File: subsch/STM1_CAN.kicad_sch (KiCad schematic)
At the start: 13 parts, among them U7 STM32F072C8Tx, U8 TJA1051T-3

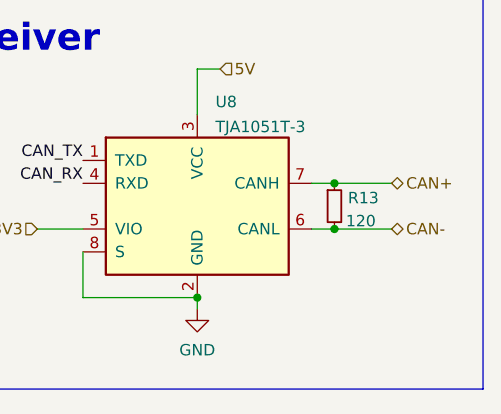
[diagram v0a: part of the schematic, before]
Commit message: Change routings&Add ESD for UART and CAN&Add 5V protection and pull-resistance for GPIO
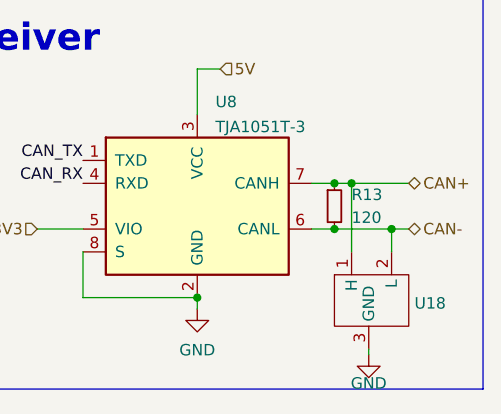
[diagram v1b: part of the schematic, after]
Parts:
- added U18: ~, Package_TO_SOT_SMD:SOT-23-3, symbol Extra IC:PESD1CAN
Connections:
- net CAN+: now also U18.1 (H)
- net CAN-: now also U18.2 (L)
- net GND: now also U18.3 (GND)
